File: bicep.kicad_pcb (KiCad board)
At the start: 4 copper layers, 70 x 85 mm, 61 parts, among them J1 DEBUG, J10 BATT, J11 USB_B_Micro, J12 BATT, J2 QWIIC, J3 QWIIC, J4 I2C, J5 SERIAL1, J6 SERIAL2, J7 ANALOG, J8 MISC, J9 DATA, Q1 2N7002, Q2 DMG3401, SW1 RESET, SW2 POWER, U1 ATSAMD21G18A-A, U2 RFM95CW, U3 MCP73831-2, U4 AP2112K-3.3, Y1 32.768K-12.5p

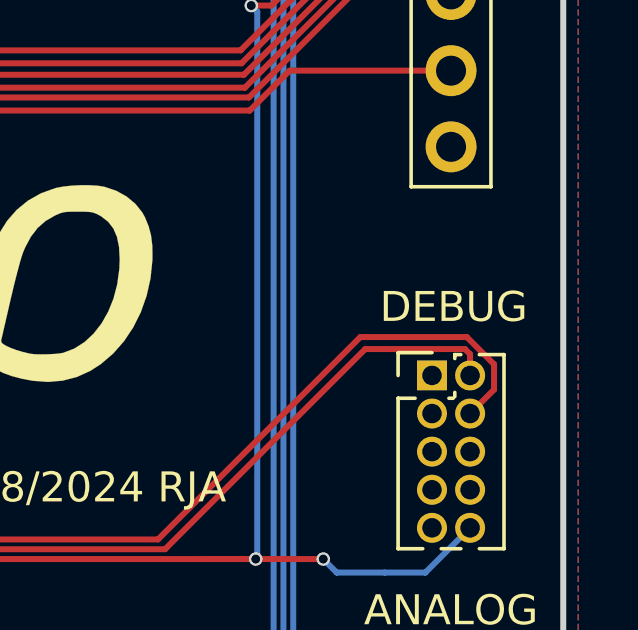
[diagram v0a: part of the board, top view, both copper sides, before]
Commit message: Added shroud to 3d rendering of Cortex Debug connector
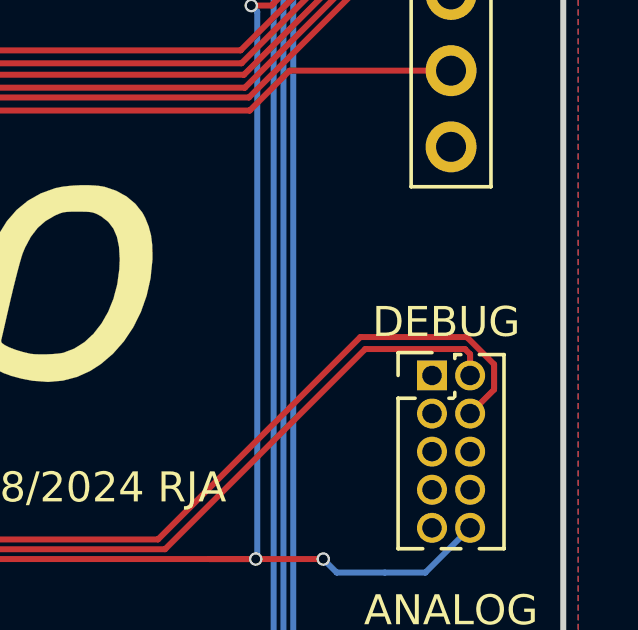
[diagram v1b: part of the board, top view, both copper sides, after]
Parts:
- J1: footprint Connector_PinHeader_1.27mm:PinHeader_2x05_P1.27mm_Vertical -> MyLib:CortexDebug
- U2: value RFM95CW -> RFM95W-915S2
